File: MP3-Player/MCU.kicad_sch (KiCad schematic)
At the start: 2 parts, among them J201 Conn_ARM_SWD_TagConnect_TC2030, U201 STM32F411CEUx

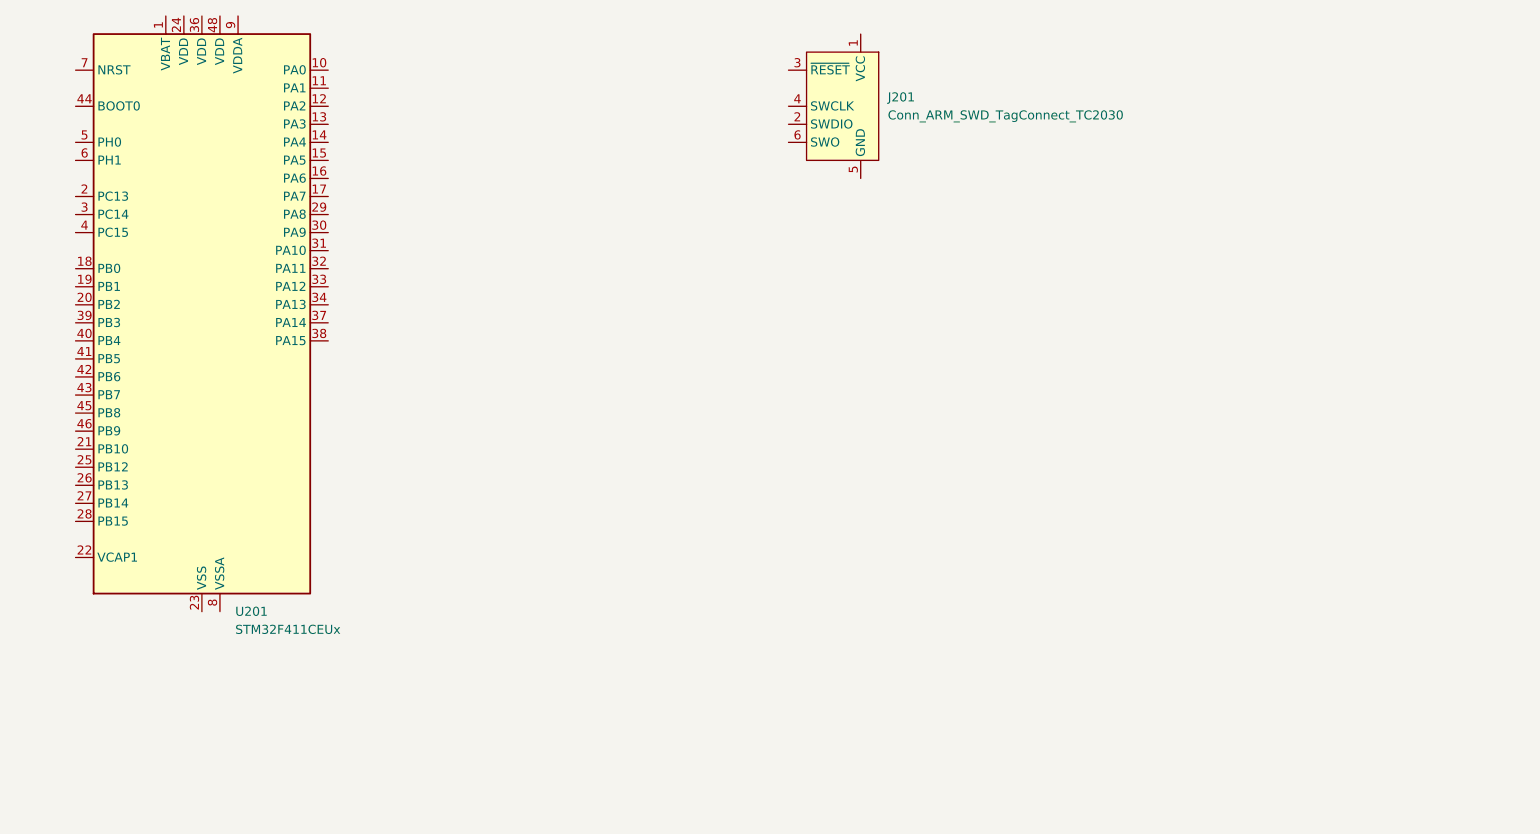
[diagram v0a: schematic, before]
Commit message: Finished cookie-cutter mcu routing
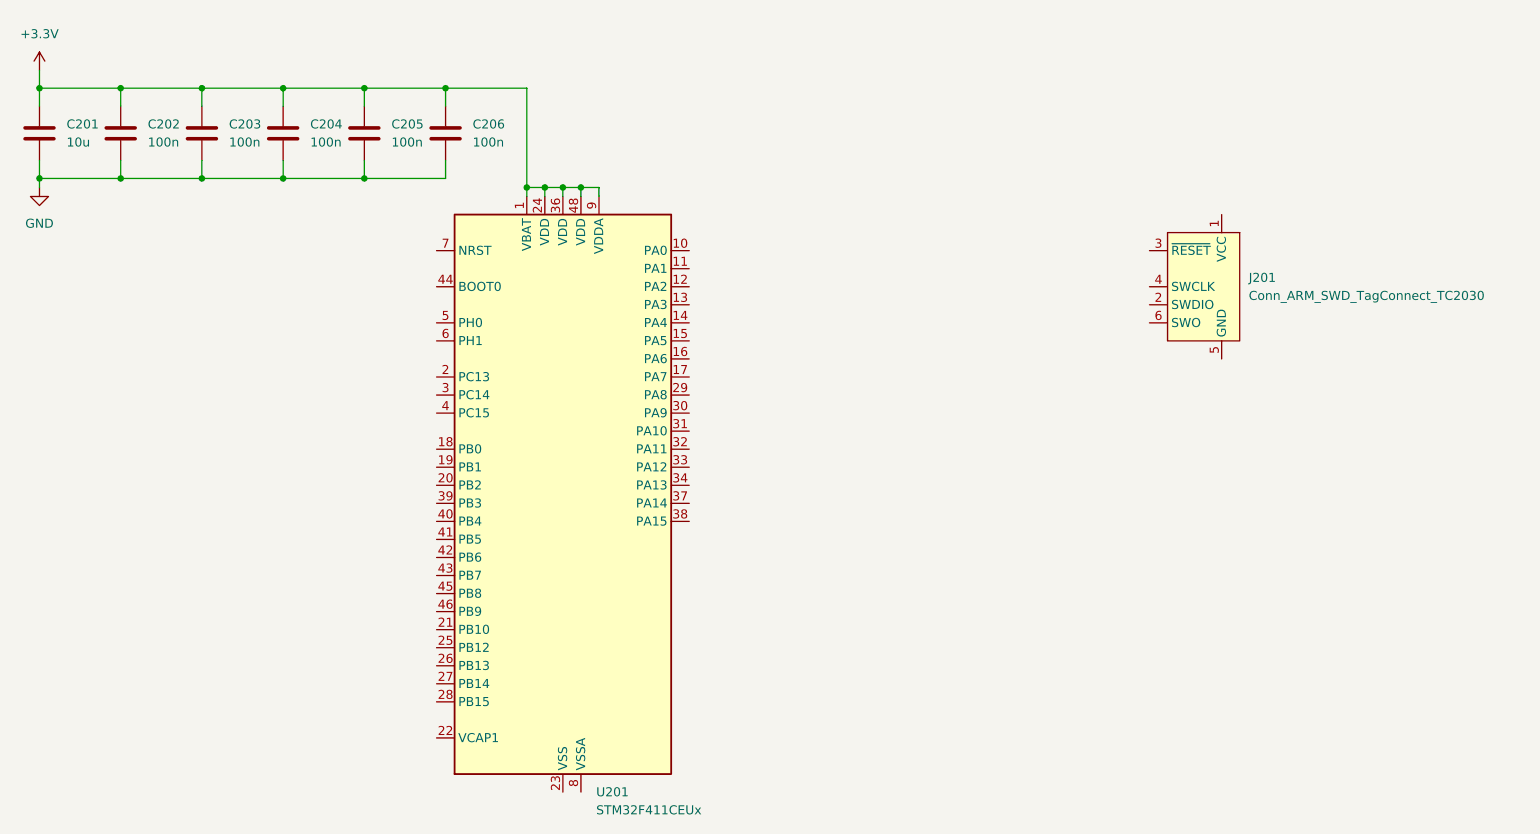
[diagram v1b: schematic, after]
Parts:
- added C201: 10u, symbol Device:C
- added C202, C203, C204, C205, C206: 100n, symbol Device:C
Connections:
- net +3.3V: now reaches U201.1 (VBAT)
- net +3.3V: now also U201.24 (VDD), U201.36 (VDD), U201.48 (VDD), U201.9 (VDDA), C201.1, C202.1, C203.1, C204.1, C205.1, C206.1
- new net GND: C201.2, C202.2, C203.2, C204.2, C205.2, C206.2
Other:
- moved on the sheet: J201, U201
